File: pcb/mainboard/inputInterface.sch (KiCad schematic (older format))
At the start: 19 parts

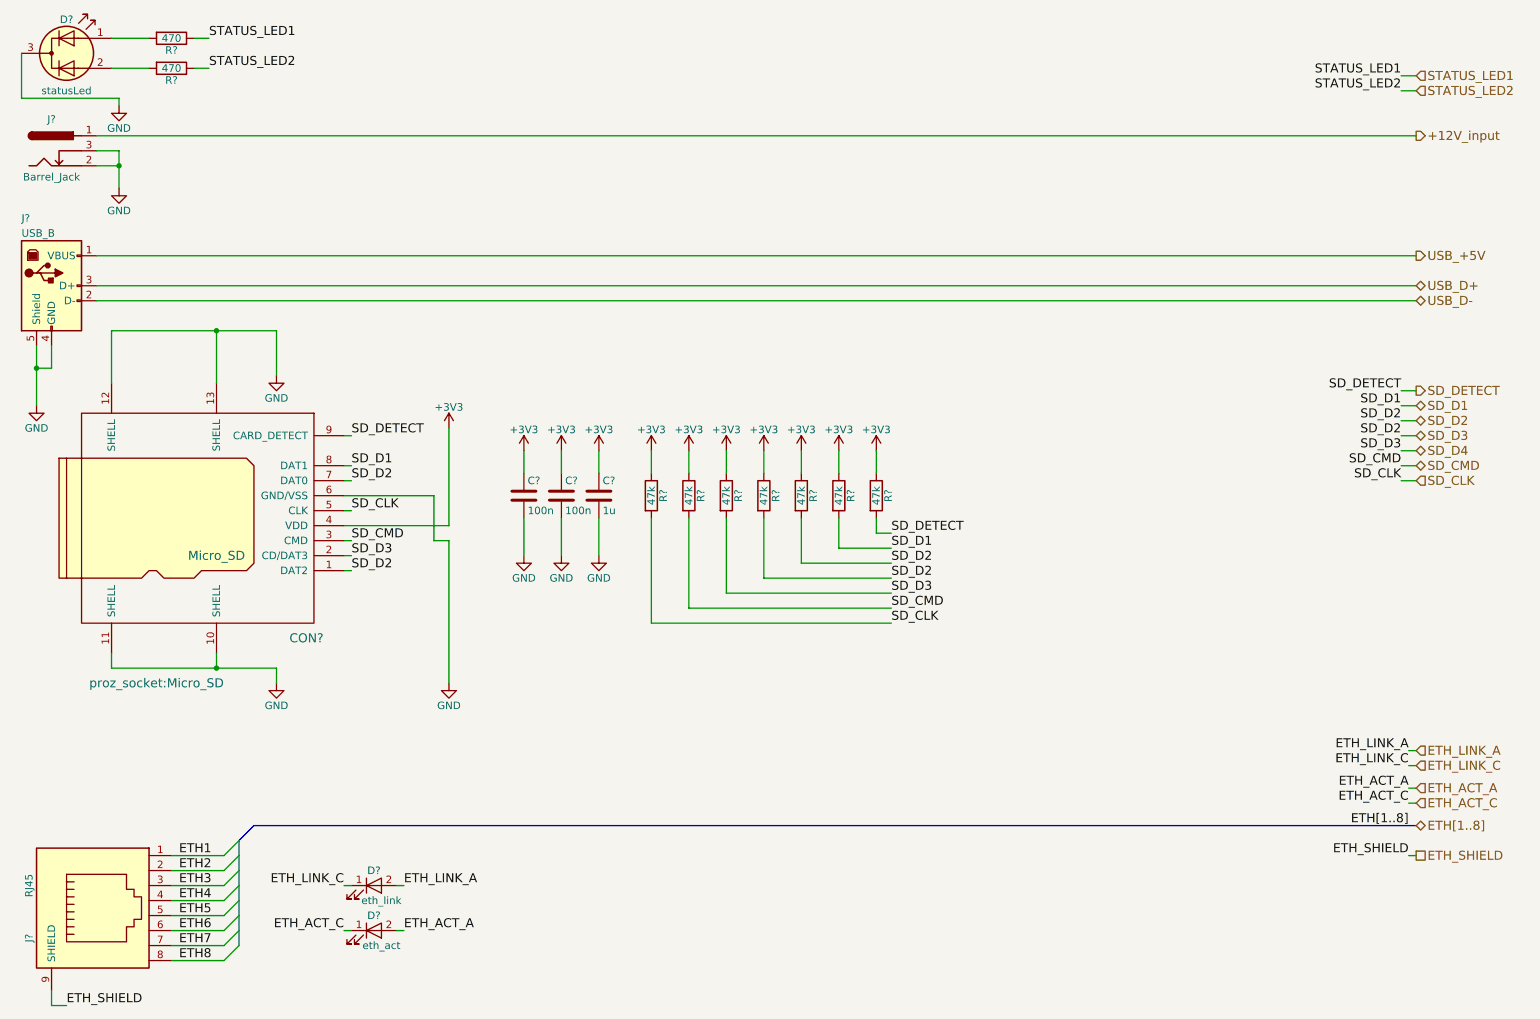
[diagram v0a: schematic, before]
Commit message: worked on PoE regulator
Added the SRAM
Added an EEPROM and a FLASH as nonvolatileMemory
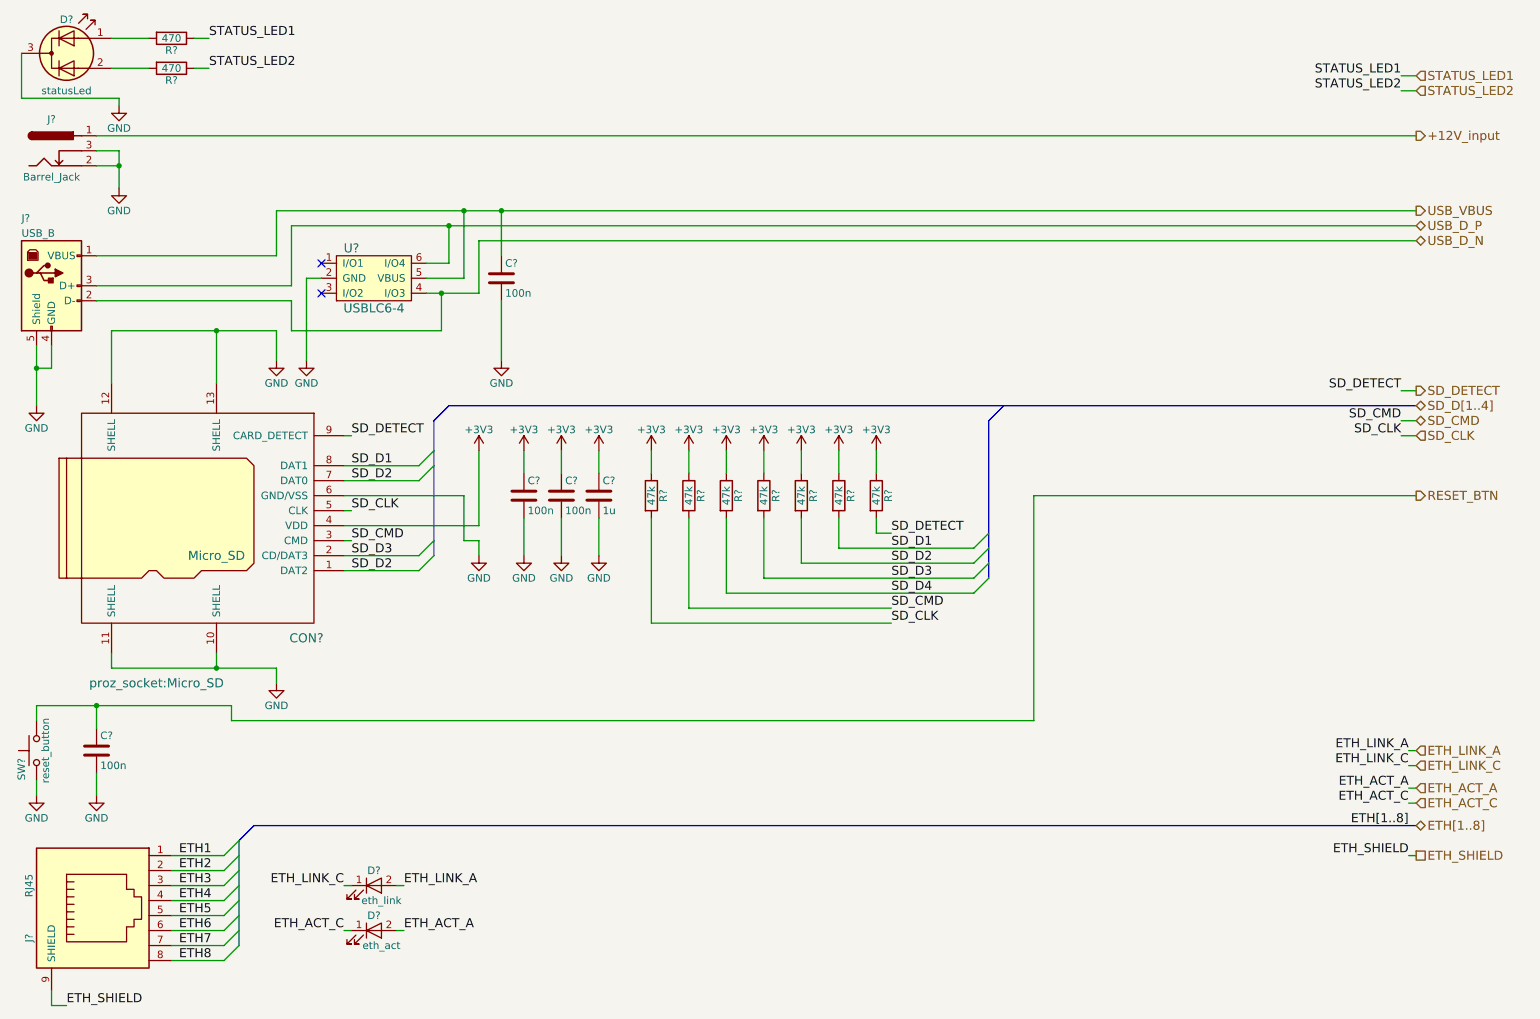
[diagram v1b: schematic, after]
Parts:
- added C? (x2): 100n, symbol C
- added SW?: reset_button, symbol SW_Push
- added U?: USBLC6-4, symbol USBLC6-4
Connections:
- net GND: now also C?.2, C?.2, SW?.2, U?.2 (GND)
- net SD_D2: no longer CON?.2 (CD/DAT3), R?.2, R?.2
- net USB_+5V renamed USB_VBUS
- net USB_VBUS: now also C?.1, U?.5 (VBUS)
- net USB_D+ renamed USB_D_P
- net USB_D_P: now also U?.6 (I/O4)
- net USB_D- renamed USB_D_N
- net USB_D_N: now also U?.4 (I/O3)
- new net RESET_BTN: C?.1, SW?.1
- new net SD_D3: CON?.2 (CD/DAT3), R?.2
- new net SD_D4: R?.2
- no-connect marks 0 -> 2
